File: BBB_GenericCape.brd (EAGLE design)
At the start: 86.3 x 55.5 mm, 3 parts, among them J1 CON_HEADER_2X08SHROUDED, J2 CON_HEADER_2X05-PTH+SHROUDED_A

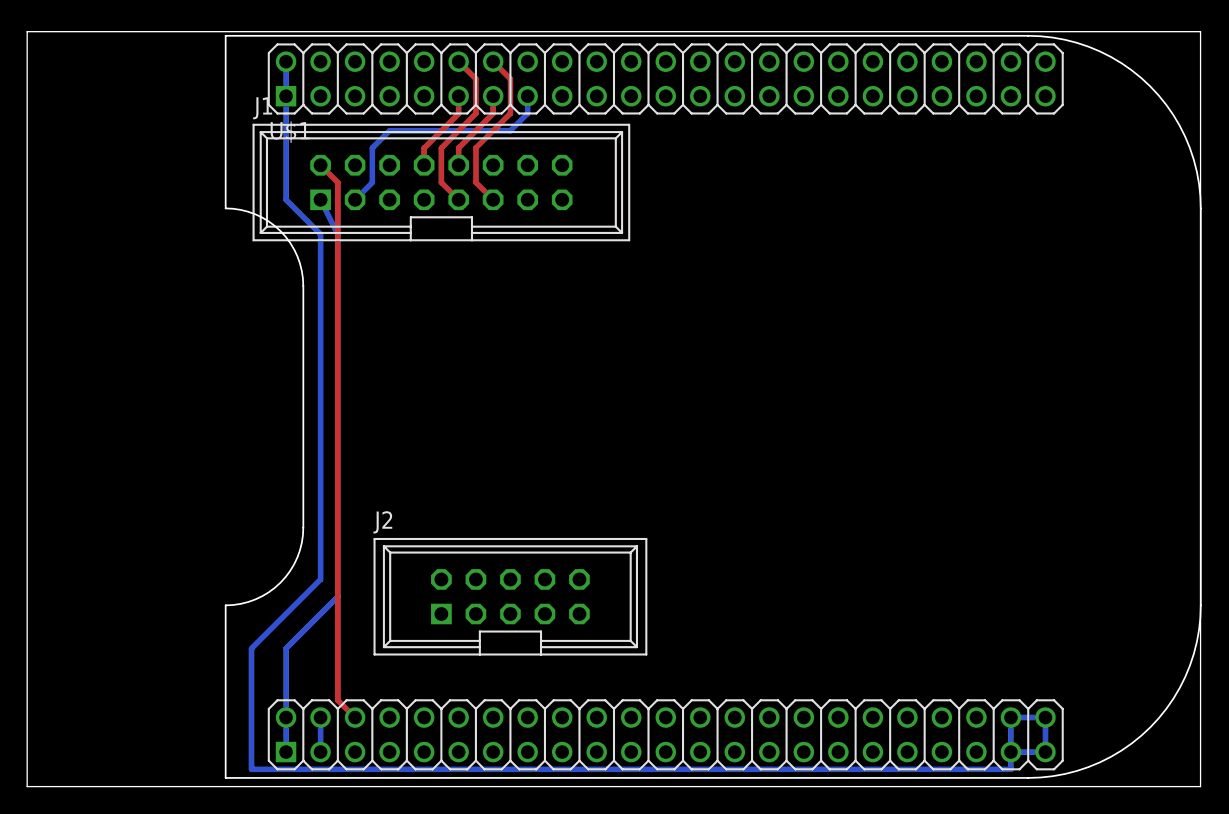
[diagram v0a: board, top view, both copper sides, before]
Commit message: fixed bbb cape issue, did something with cable splice
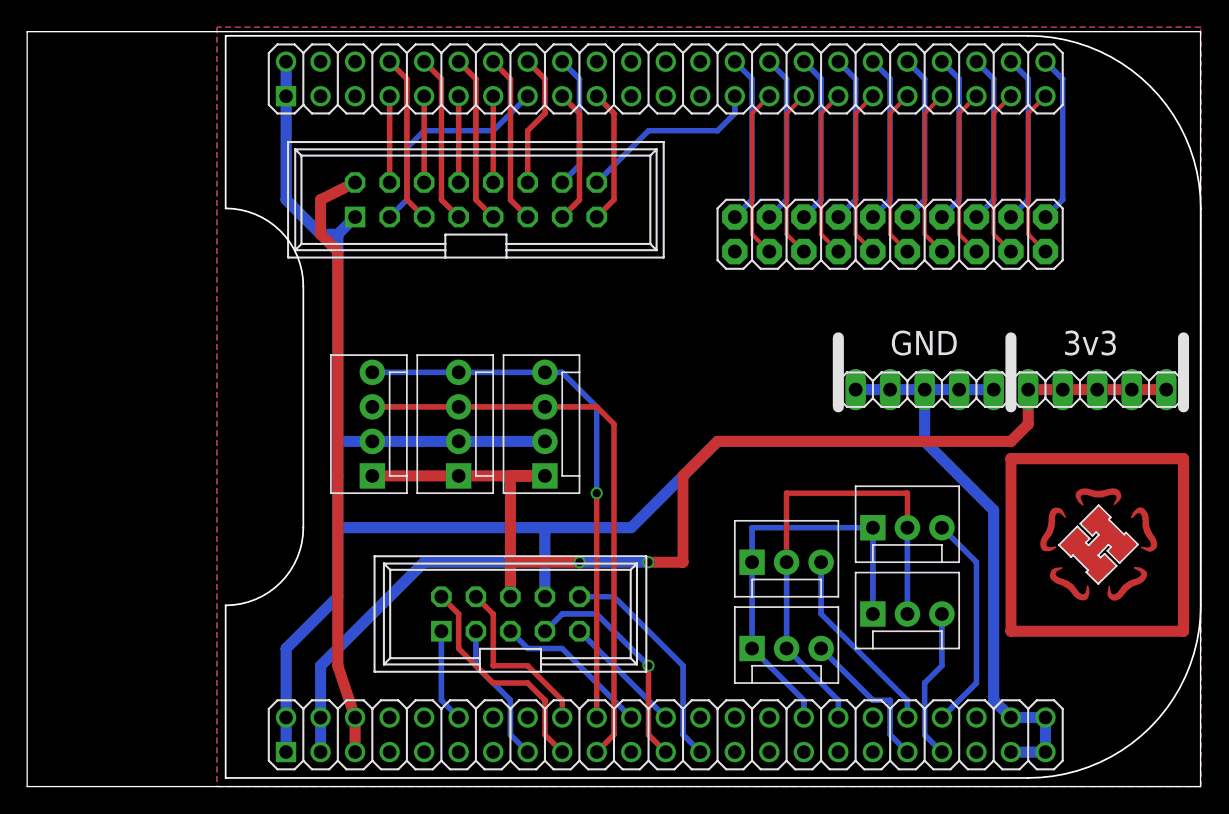
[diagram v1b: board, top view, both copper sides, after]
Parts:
- added JGP: M10X2, SparkFun-Connectors:2X10
- added JP1, JP2, JP3, JP4: (no value), SparkFun-Connectors:MOLEX-1X3
- added JP5, JP6, JP7: (no value), SparkFun-Connectors:MOLEX-1X4
- added JPWR: (no value), pinhead:1X10
- added U$4: (no value), YHSLogo:YHSLOGO_SMALL_FANCY
- moved J1 2.84 mm to (31.8, 43.2)
- moved J2 1.27 mm to (35.6, 12.7)
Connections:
- net N$3 renamed HDBUS_RS
- net N$4 renamed HDBUS_4
- net N$5 renamed HDBUS_7
- net N$6 renamed HDBUS_6
- net N$7 renamed HDBUS_5
- removed net AIN0: U$1.85
- removed net N$1: J1.1, U$1.47, U$1.48
- removed net N$2: J1.2, U$1.52
- removed net VDD_3V3EXP: U$1.49, U$1.50
- new net 3V3: J2.6, JP5.1, JP6.1, JP7.1, JPWR.10, JPWR.6, JPWR.7, JPWR.8, JPWR.9, U$1.49, U$1.50
- new net AIN_0: JP4.3, U$1.85
- new net AIN_1: JP1.3, U$1.86
- new net AIN_2: JP2.3, U$1.83
- new net AIN_3: JP3.3, U$1.84
- new net GND_ADC: JP1.2, JP2.2, JP3.2, JP4.2, U$1.80
- new net HDBUS_0: J1.4, U$1.7
- new net HDBUS_1: J1.5, U$1.8
- new net HDBUS_2: J1.6, U$1.9
- new net HDBUS_3: J1.7, U$1.10
- new net HDEN_0: J1.12, U$1.16
- new net HDEN_1: J1.13, U$1.17
- new net HDEN_2: J1.14, U$1.18
- new net HDEN_3: J1.15, U$1.19
- new net HDEN_4: J1.16, U$1.27
- new net I2C_SCL: JP5.3, JP6.3, JP7.3, U$1.65
- new net I2C_SDA: JP5.4, JP6.4, JP7.4, U$1.66
- new net NC1: JGP.1
- new net NOKIA_BUS_CLK: J2.5, U$1.68
- new net NOKIA_BUS_D0: J2.3, U$1.61
- new net NOKIA_BUS_D1: J2.4, U$1.64
- new net NOKIA_BUS_EN_1: J2.7, U$1.69
- new net NOKIA_BUS_EN_2: J2.9, U$1.70
- new net NOKIA_BUS_EN_3: J2.10, U$1.71
- new net NOKIA_BUS_HARD_CS: J2.2, U$1.63
- new net NOKIA_BUS_RESET: J2.1, U$1.58
- new net P8_28: JGP.2, U$1.28
- new net P8_29: JGP.3, U$1.29
- new net P8_30: JGP.4, U$1.30
- new net P8_31: JGP.5, U$1.31
- new net P8_32: JGP.6, U$1.32
- new net P8_33: JGP.7, U$1.33
- new net P8_34: JGP.8, U$1.34
- new net P8_35: JGP.9, U$1.35
- new net P8_36: JGP.10, U$1.36
- new net P8_37: JGP.11, U$1.37
- new net P8_38: JGP.12, U$1.38
- new net P8_39: JGP.13, U$1.39
- new net P8_40: JGP.14, U$1.40
- new net P8_41: JGP.15, U$1.41
- new net P8_42: JGP.16, U$1.42
- new net P8_43: JGP.17, U$1.43
- new net P8_44: JGP.18, U$1.44
- new net P8_45: JGP.19, U$1.45
- new net P8_46: JGP.20, U$1.46
- new net VDD_ADC: JP1.1, JP2.1, JP3.1, JP4.1, U$1.78
- net GND: now also J1.1, J2.8, JP5.2, JP6.2, JP7.2, JPWR.1, JPWR.2, JPWR.3, JPWR.4, JPWR.5, U$1.47, U$1.48
- net VDD_5V: now also J1.2, U$1.52
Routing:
- net 3V3: track 0.00 -> 108.9 mm, vias 0 -> 2
- net LOGO_GUARD_3V3: track 0.00 -> 50.8 mm
- net GND: track 122.5 -> 167.2 mm
- net VDD_5V: track 0.00 -> 44.2 mm
- net I2C_SCL: track 0.00 -> 43.0 mm
- net N$1: track 42.5 -> 0.00 mm
- net N$2: track 41.7 -> 0.00 mm
- net I2C_SDA: track 0.00 -> 40.4 mm, vias 0 -> 1
- net GND_ADC: track 0.00 -> 35.9 mm
- net VDD_ADC: track 0.00 -> 30.8 mm
- net NOKIA_BUS_EN_3: track 0.00 -> 16.6 mm
- net NOKIA_BUS_EN_1: track 0.00 -> 16.6 mm, vias 0 -> 1
- net NOKIA_BUS_HARD_CS: track 0.00 -> 16.6 mm
- net AIN_1: track 0.00 -> 16.1 mm
- net AIN_3: track 0.00 -> 14.1 mm
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- added copper zone on layer 1, net 3V3
- added copper zone on layer 16, net GND
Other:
- board text added: "28 30 32 34 36 38 40 42 44 46"
- board text added: "3v3"
- board text added: "ADCs"
- board text added: "AIN"
- board text added: "GND"
- board text added: "HD44780 Bus"
- board text added: "I2C"
- board text added: "IN_0"
- board text added: "IN_1"
- board text added: "IN_2"
- board text added: "IN_3"
- board text added: "N/C 29 31 33 35 37 39 41 43 45"
- board text added: "Nokia Bus"
- board text added: "P8 GPIOs"
- board text added: "SCL"
- board text added: "SDA"
- board text added: "VCC"
